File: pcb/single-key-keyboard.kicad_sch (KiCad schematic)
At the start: 25 parts, among them J2 Conn_01x05, P1 USB_C_Plug_USB2.0, SW1 SW_Push, SW2 SW_SPST, U1 ATtiny416-M

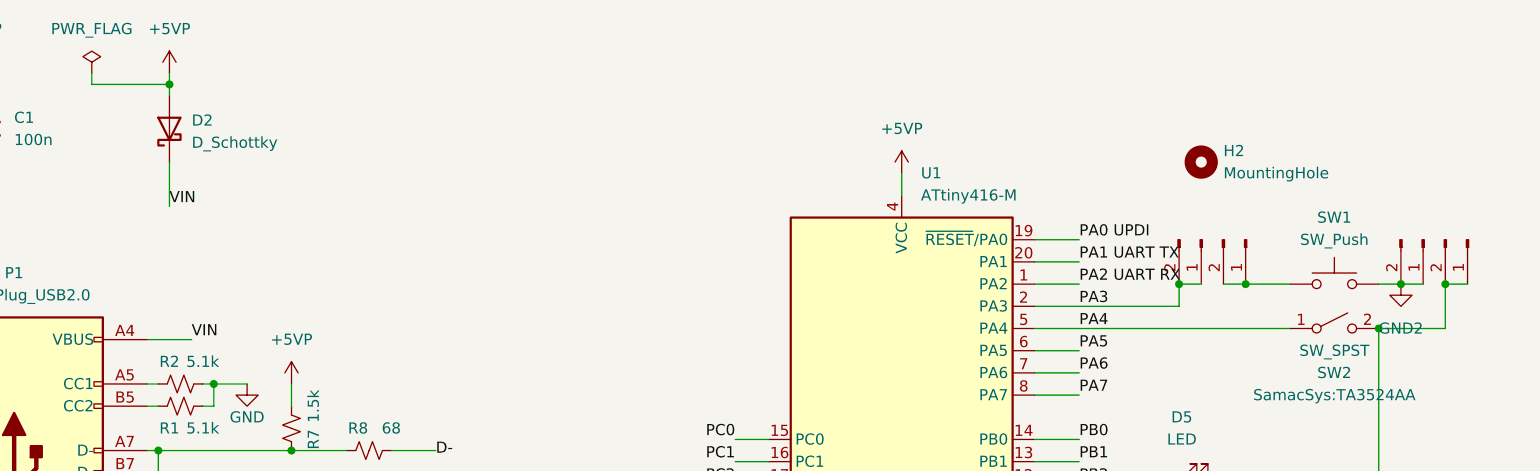
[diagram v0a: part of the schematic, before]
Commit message: Code compiles and pick correct pcb version
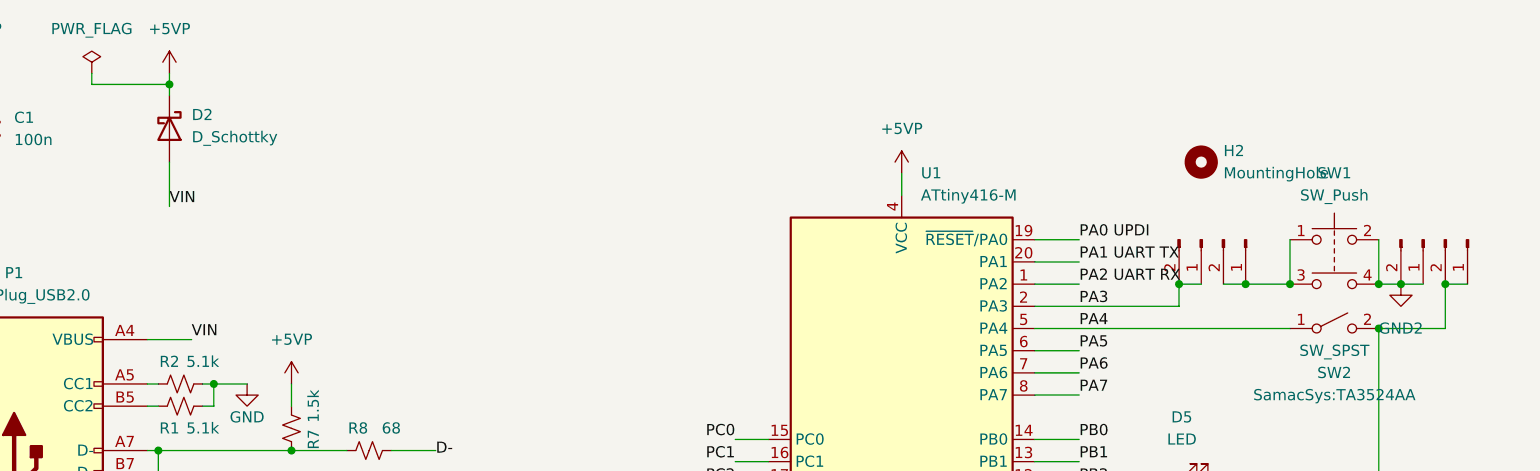
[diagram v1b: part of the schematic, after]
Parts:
- removed SW1: SW_Push, keyswitches:Kailh_socket_MX_optional, symbol Switch:SW_Push
- added SW1: SW_Push, keyswitches:Kailh_socket_MX_optional, symbol Switch:SW_Push_Dual
- D2: footprint Diode_SMD:D_0402_1005Metric -> Diode_SMD:D_SOD-323
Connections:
- net +5VP: now also D2.1 (K); no longer D2.2 (A)
- net GND2: now also SW1.2, SW1.4
- net VIN: now also D2.2 (A); no longer D2.1 (K)
- net at TP1.1 (Pin_1), TP1.2 (Pin_2): now also SW1.1, SW1.3
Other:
- moved on the sheet: D2
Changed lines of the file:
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@@
   (junction (at 62.23 62.23) (diameter 0) (color 0 0 0 0)
   )
+  (junction (at 195.58 50.8) (diameter 0) (color 0 0 0 0)
+  )
   (junction (at 203.2 50.8) (diameter 0) (color 0 0 0 0)
+  )
+  (junction (at 185.42 50.8) (diameter 0) (color 0 0 0 0)
   )
   (no_connect (at 54.61 85.09))
@@
     (stroke (width 0) (type default))
   )
+  (wire (pts (xy 195.58 45.72) (xy 195.58 50.8))
+    (stroke (width 0) (type default))
+  )
   (wire (pts (xy 55.88 69.85) (xy 71.12 69.85))
     (stroke (width 0) (type default))
@@
   )
   (wire (pts (xy 180.34 95.25) (xy 175.26 95.25))
+    (stroke (width 0) (type default))
+  )
+  (wire (pts (xy 185.42 45.72) (xy 185.42 50.8))
     (stroke (width 0) (type default))
   )
@@
     )
   )
-  (symbol (lib_id "Switch:SW_Push") (at 190.5 50.8 0) (unit 1)
-    (in_bom yes) (on_board yes) (dnp no)
-    (property "Reference" "SW1" (at 190.5 43.18 0)
-      (effects (font (size 1.27 1.27)))
-    )
-    (property "Value" "SW_Push" (at 190.5 45.72 0)
-      (effects (font (size 1.27 1.27)))
-    )
-    (property "Footprint" "keyswitches:Kailh_socket_MX_optional" (at 190.5 45.72 0)
-      (effects (font (size 1.27 1.27)) hide)
-    )
-    (property "Datasheet" "~" (at 190.5 45.72 0)
-      (effects (font (size 1.27 1.27)) hide)
-    )
-    (pin "1")
-    (pin "2")
-    (instances
-      (project "single-key-keyboard"
-        (path "/319be8ac-c812-4dc1-a038-09f5b0d482b5"
-          (reference "SW1") (unit 1)
-        )
-      )
-    )
-  )
   (symbol (lib_id "power:+5VP") (at 35.56 26.67 0) (unit 1)
     (in_bom yes) (on_board yes) (dnp no) (fields_autoplaced)
@@
         (path "/319be8ac-c812-4dc1-a038-09f5b0d482b5"
           (reference "R4") (unit 1)
+        )
+      )
+    )
+  )
+  (symbol (lib_id "Switch:SW_Push_Dual") (at 190.5 45.72 0) (unit 1)
+    (in_bom yes) (on_board yes) (dnp no)
+    (property "Reference" "SW1" (at 190.5 38.1 0)
+      (effects (font (size 1.27 1.27)))
+    )
+    (property "Value" "SW_Push" (at 190.5 40.64 0)
+      (effects (font (size 1.27 1.27)))
+    )
+    (property "Footprint" "keyswitches:Kailh_socket_MX_optional" (at 190.5 40.64 0)
+      (effects (font (size 1.27 1.27)) hide)
+    )
+    (property "Datasheet" "~" (at 190.5 40.64 0)
+      (effects (font (size 1.27 1.27)) hide)
+    )
+    (pin "1")
+    (pin "2")
+    (pin "3")
+    (pin "4")
+    (instances
+      (project "single-key-keyboard"
+        (path "/319be8ac-c812-4dc1-a038-09f5b0d482b5"
+          (reference "SW1") (unit 1)
         )
       )
@@
     )
   )
-  (symbol (lib_id "Device:D_Schottky") (at 57.15 33.02 90) (unit 1)
-    (in_bom yes) (on_board yes) (dnp no) (fields_autoplaced)
-    (property "Reference" "D2" (at 59.69 32.0675 90)
-      (effects (font (size 1.27 1.27)) (justify right))
-    )
-    (property "Value" "D_Schottky" (at 59.69 34.6075 90)
-      (effects (font (size 1.27 1.27)) (justify right))
-    )
-    (property "Footprint" "Diode_SMD:D_0402_1005Metric" (at 57.15 33.02 0)
-      (effects (font (size 1.27 1.27)) hide)
-    )
+  (symbol (lib_id "Device:D_Schottky") (at 57.15 33.02 270) (unit 1)
+    (in_bom yes) (on_board yes) (dnp no) (fields_autoplaced)
+    (property "Reference" "D2" (at 59.69 31.4325 90)
+      (effects (font (size 1.27 1.27)) (justify left))
+    )
+    (property "Value" "D_Schottky" (at 59.69 33.9725 90)
+      (effects (font (size 1.27 1.27)) (justify left))
+    )
+    (property "Footprint" "Diode_SMD:D_SOD-323" (at 57.15 33.02 0)
+      (effects (font (size 1.27 1.27)) hide)
+    )
